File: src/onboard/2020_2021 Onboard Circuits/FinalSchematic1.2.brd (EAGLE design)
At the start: 137.6 x 80 mm, 82 parts, among them IC1 MIC2937A-5.0BT, IC3 A5975D

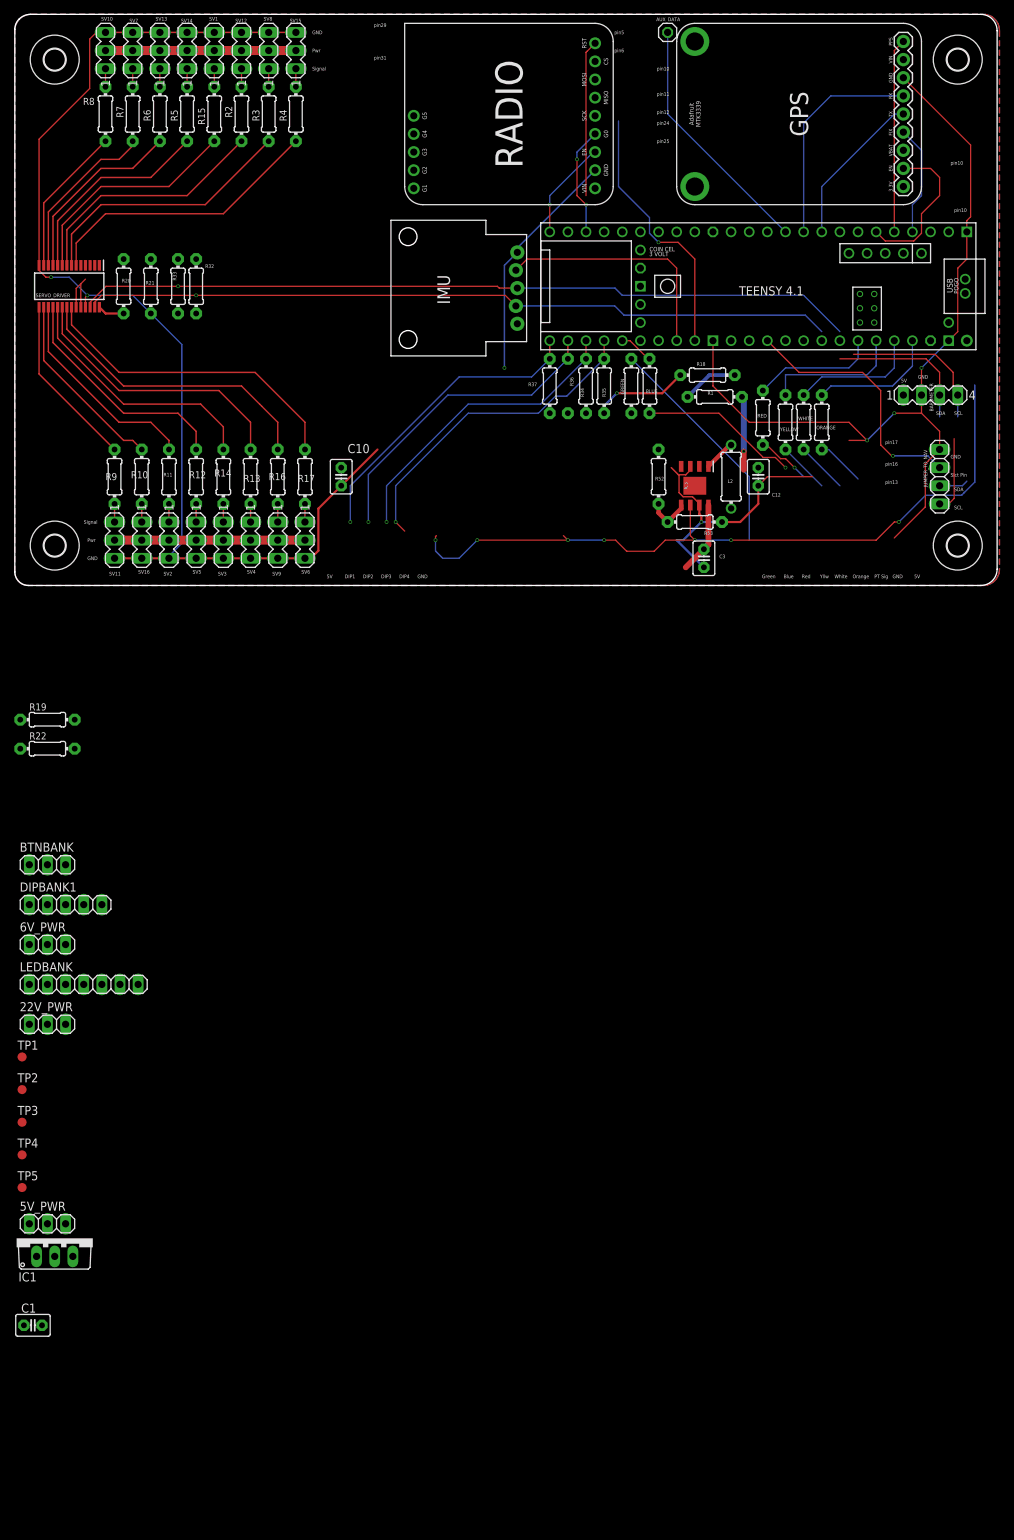
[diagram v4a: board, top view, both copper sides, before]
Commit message: Added pulldown on select pin and added wiring for aux pin
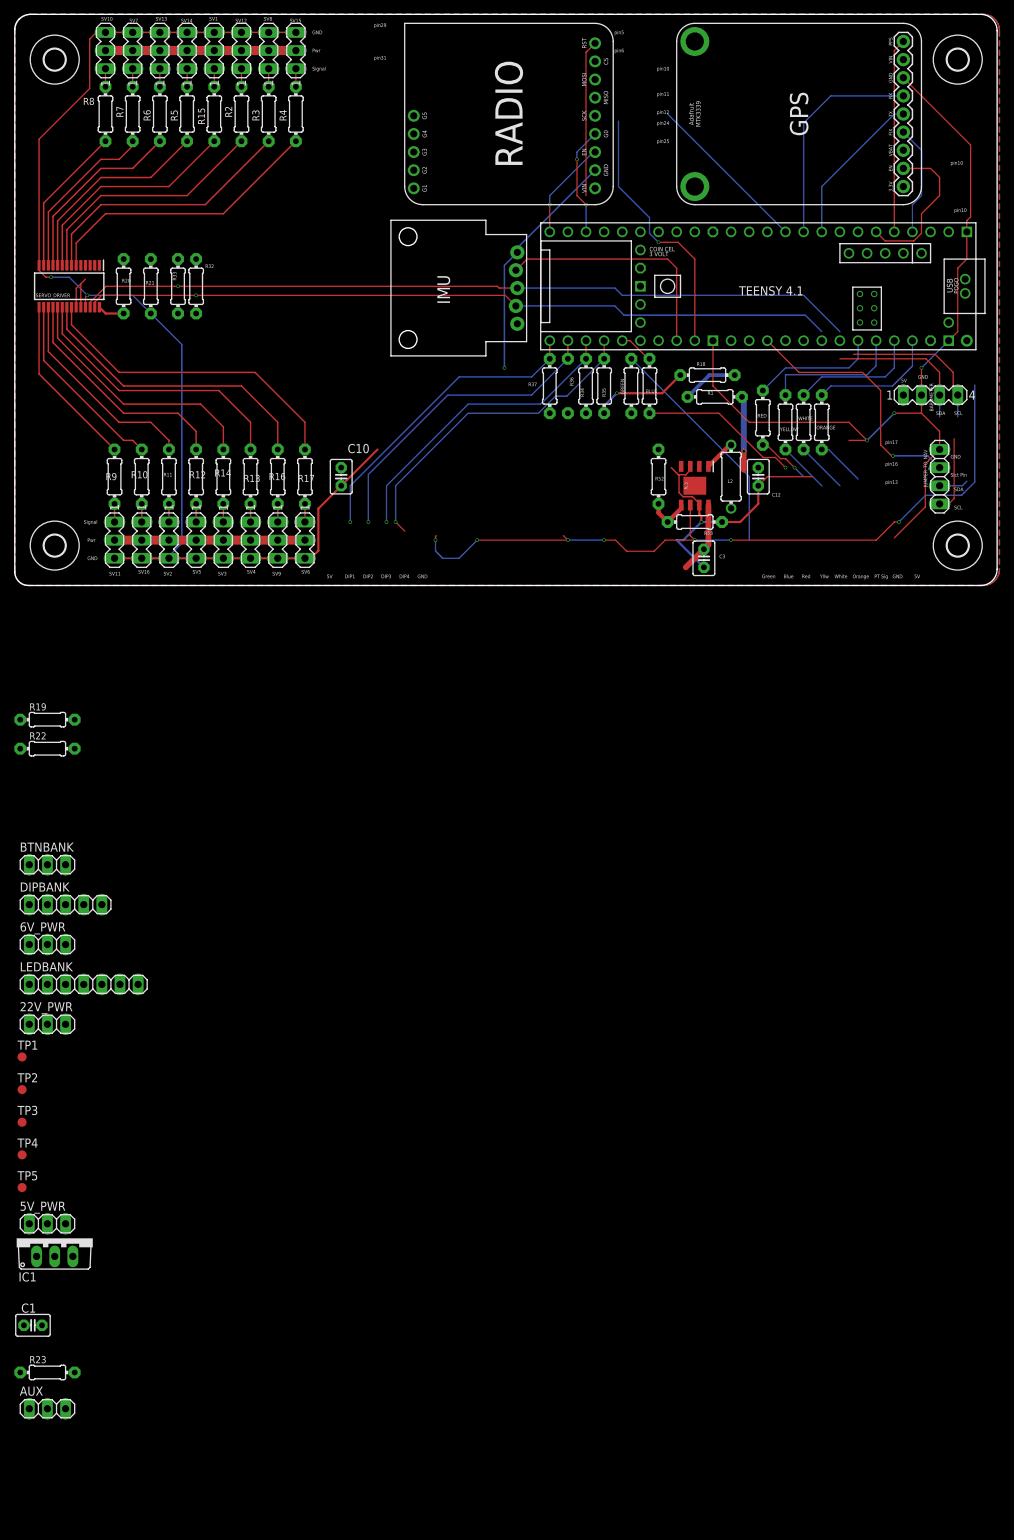
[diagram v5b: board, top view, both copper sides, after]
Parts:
- removed AUX_DATA: (no value), pinhead:1X01
- added AUX: (no value), pinhead:1X03
- added R23: 2.2k, adafruit:0204/7
- renumbered DIPBANK1 to DIPBANK
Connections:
- new net AUX: AUX.3, TEENSY4.1.27-A13/SCK1
- new net N$4: AUX.2
- net AUX_DATA: no longer AUX_DATA.1
- net GND: now also AUX.1, R23.1
- net SELECT_PIN: now also R23.2
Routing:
- net AUX_DATA: track 34.8 -> 23.3 mm
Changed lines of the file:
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@@
 <attribute name="VALUE" x="65.3596" y="13.4366" size="0.508" layer="27" ratio="10" rot="R180"/>
-</element>
-<element name="AUX_DATA" library="pinhead" library_urn="urn:adsk.eagle:library:325" package="1X01" package3d_urn="urn:adsk.eagle:package:22485/2" value="" x="55.88" y="77.47" smashed="yes" rot="R270">
-<attribute name="NAME" x="54.2798" y="79.0448" size="0.508" layer="25" ratio="10"/>
-<attribute name="POPULARITY" value="64" x="55.88" y="77.47" size="1.778" layer="27" rot="R270" display="off"/>
-<attribute name="VALUE" x="52.705" y="78.74" size="1.27" layer="27" rot="R270"/>
 </element>
 <element name="JUMPER_TO_NAV" library="pinhead" library_urn="urn:adsk.eagle:library:325" package="1X04" package3d_urn="urn:adsk.eagle:package:22407/2" value="" x="93.98" y="15.24" smashed="yes" rot="R270">
@@
 <attribute name="VALUE" x="-34.798" y="-42.291" size="1.27" layer="27"/>
 </element>
-<element name="DIPBANK1" library="pinhead" library_urn="urn:adsk.eagle:library:325" package="1X05" package3d_urn="urn:adsk.eagle:package:22469/2" value="" x="-28.448" y="-44.704" smashed="yes">
+<element name="DIPBANK" library="pinhead" library_urn="urn:adsk.eagle:library:325" package="1X05" package3d_urn="urn:adsk.eagle:package:22469/2" value="" x="-28.448" y="-44.704" smashed="yes">
 <attribute name="NAME" x="-34.8742" y="-42.8752" size="1.27" layer="25" ratio="10"/>
 <attribute name="POPULARITY" value="69" x="-28.448" y="-44.704" size="1.778" layer="27" display="off"/>
@@
 <attribute name="POPULARITY" value="38" x="-33.02" y="-103.632" size="1.778" layer="27" display="off"/>
 <attribute name="VALUE" x="-34.671" y="-106.68" size="1.27" layer="27" ratio="10"/>
+</element>
+<element name="R23" library="adafruit" library_urn="urn:adsk.eagle:library:420" package="0204/7" package3d_urn="urn:adsk.eagle:package:6240596/1" value="2.2k" x="-30.988" y="-110.236" smashed="yes">
+<attribute name="NAME" x="-33.528" y="-108.9406" size="0.9906" layer="25" ratio="12"/>
+<attribute name="VALUE" x="-32.6136" y="-110.7186" size="0.9906" layer="27" ratio="12"/>
+</element>
+<element name="AUX" library="pinhead" library_urn="urn:adsk.eagle:library:325" package="1X03" package3d_urn="urn:adsk.eagle:package:22458/2" value="" x="-30.988" y="-115.316" smashed="yes">
+<attribute name="NAME" x="-34.8742" y="-113.4872" size="1.27" layer="25" ratio="10"/>
+<attribute name="POPULARITY" value="92" x="-30.988" y="-115.316" size="1.778" layer="27" display="off"/>
+<attribute name="VALUE" x="-34.798" y="-118.491" size="1.27" layer="27"/>
 </element>
 </elements>
@@
 <contactref element="R33" pad="2"/>
 <contactref element="BTNBANK" pad="3"/>
-<contactref element="DIPBANK1" pad="5"/>
+<contactref element="DIPBANK" pad="5"/>
 <contactref element="SV9" pad="2"/>
 <contactref element="SV6" pad="2"/>
@@
 <wire x1="11.43" y1="13.97" x2="11.43" y2="8.89" width="0.1524" layer="16"/>
 <via x="11.43" y="8.89" extent="1-16" drill="0.35"/>
-<contactref element="DIPBANK1" pad="4"/>
+<contactref element="DIPBANK" pad="4"/>
 <wire x1="11.43" y1="8.89" x2="-25.908" y2="-44.704" width="0" layer="19" extent="1-1"/>
 </signal>
@@
 <via x="17.78" y="8.89" extent="1-16" drill="0.35"/>
 <wire x1="17.78" y1="8.89" x2="19.05" y2="7.62" width="0.1524" layer="1"/>
-<contactref element="DIPBANK1" pad="1"/>
+<contactref element="DIPBANK" pad="1"/>
 <wire x1="19.05" y1="7.62" x2="-33.528" y2="-44.704" width="0" layer="19" extent="1-1"/>
 </signal>
@@
 <wire x1="13.97" y1="15.55053125" x2="13.97" y2="8.89" width="0.1524" layer="16"/>
 <wire x1="36.83" y1="26.67" x2="25.08946875" y2="26.67" width="0.1524" layer="16"/>
-<contactref element="DIPBANK1" pad="3"/>
+<contactref element="DIPBANK" pad="3"/>
 <wire x1="13.97" y1="8.89" x2="-28.448" y2="-44.704" width="0" layer="19" extent="1-1"/>
 </signal>
@@
 <wire x1="16.51" y1="13.97" x2="16.51" y2="8.89" width="0.1524" layer="16"/>
 <via x="16.51" y="8.89" extent="1-16" drill="0.35"/>
-<contactref element="DIPBANK1" pad="2"/>
+<contactref element="DIPBANK" pad="2"/>
 <wire x1="16.51" y1="8.89" x2="-30.988" y2="-44.704" width="0" layer="19" extent="1-1"/>
 </signal>
@@
 <contactref element="5V_PWR" pad="3"/>
 <contactref element="IC1" pad="2"/>
+<contactref element="R23" pad="1"/>
+<contactref element="AUX" pad="1"/>
+<wire x1="-34.798" y1="-110.236" x2="-33.528" y2="-115.316" width="0" layer="19" extent="1-1"/>
+<wire x1="-29.972" y1="-93.98" x2="-34.798" y2="-110.236" width="0" layer="19" extent="1-1"/>
+<wire x1="-28.448" y1="-89.408" x2="-29.972" y2="-93.98" width="0" layer="19" extent="1-1"/>
+<wire x1="-28.448" y1="-61.468" x2="-28.448" y2="-89.408" width="0" layer="19" extent="1-1"/>
+<wire x1="-33.528" y1="-55.88" x2="-28.448" y2="-61.468" width="0" layer="19" extent="1-1"/>
+<wire x1="-28.448" y1="-50.292" x2="-33.528" y2="-55.88" width="0" layer="19" extent="1-1"/>
+<wire x1="-34.798" y1="-22.86" x2="-28.448" y2="-50.292" width="0" layer="19" extent="1-1"/>
+<wire x1="-34.798" y1="-18.796" x2="-34.798" y2="-22.86" width="0" layer="19" extent="1-1"/>
+<wire x1="-21.59" y1="3.81" x2="-34.798" y2="-18.796" width="0" layer="19" extent="1-1"/>
+<wire x1="33.02" y1="30.48" x2="15.24" y2="19.05" width="0" layer="19" extent="1-1"/>
+<wire x1="39.37" y1="24.13" x2="33.02" y2="30.48" width="0" layer="19" extent="1-1"/>
+<wire x1="41.91" y1="24.13" x2="39.37" y2="24.13" width="0" layer="19" extent="1-1"/>
+<wire x1="44.45" y1="24.13" x2="41.91" y2="24.13" width="0" layer="19" extent="1-1"/>
+<wire x1="46.99" y1="24.13" x2="44.45" y2="24.13" width="0" layer="19" extent="1-1"/>
+<wire x1="46.99" y1="25.146" x2="46.99" y2="24.13" width="0" layer="19" extent="16-16"/>
+<wire x1="62.23" y1="34.29" x2="57.658" y2="29.464" width="0" layer="19" extent="1-1"/>
+<wire x1="76.2" y1="15.24" x2="81.28" y2="20.32" width="0" layer="19" extent="1-1"/>
+<wire x1="52.07" y1="41.91" x2="62.23" y2="34.29" width="0" layer="19" extent="1-1"/>
+<wire x1="83.82" y1="46.53" x2="97.79" y2="49.53" width="0" layer="19" extent="1-1"/>
 <wire x1="81.28" y1="46.53" x2="83.82" y2="46.53" width="0" layer="19" extent="1-1"/>
-<wire x1="97.79" y1="49.53" x2="83.82" y2="46.53" width="0" layer="19" extent="1-1"/>
-<wire x1="57.658" y1="29.464" x2="62.23" y2="34.29" width="0" layer="19" extent="1-1"/>
-<wire x1="46.99" y1="24.13" x2="46.99" y2="25.146" width="0" layer="19" extent="16-16"/>
-<wire x1="44.45" y1="24.13" x2="46.99" y2="24.13" width="0" layer="19" extent="1-1"/>
-<wire x1="41.91" y1="24.13" x2="44.45" y2="24.13" width="0" layer="19" extent="1-1"/>
-<wire x1="39.37" y1="24.13" x2="41.91" y2="24.13" width="0" layer="19" extent="1-1"/>
-<wire x1="76.2" y1="15.24" x2="81.28" y2="20.32" width="0" layer="19" extent="1-1"/>
-<wire x1="33.02" y1="30.48" x2="39.37" y2="24.13" width="0" layer="19" extent="1-1"/>
-<wire x1="52.07" y1="41.91" x2="62.23" y2="34.29" width="0" layer="19" extent="1-1"/>
-<wire x1="15.24" y1="19.05" x2="33.02" y2="30.48" width="0" layer="19" extent="1-1"/>
-<wire x1="-34.798" y1="-18.796" x2="-21.59" y2="3.81" width="0" layer="19" extent="1-1"/>
-<wire x1="-34.798" y1="-22.86" x2="-34.798" y2="-18.796" width="0" layer="19" extent="1-1"/>
-<wire x1="-28.448" y1="-50.292" x2="-34.798" y2="-22.86" width="0" layer="19" extent="1-1"/>
-<wire x1="-33.528" y1="-55.88" x2="-28.448" y2="-50.292" width="0" layer="19" extent="1-1"/>
-<wire x1="-28.448" y1="-61.468" x2="-33.528" y2="-55.88" width="0" layer="19" extent="1-1"/>
-<wire x1="-28.448" y1="-89.408" x2="-28.448" y2="-61.468" width="0" layer="19" extent="1-1"/>
-<wire x1="-29.972" y1="-93.98" x2="-28.448" y2="-89.408" width="0" layer="19" extent="1-1"/>
 </signal>
 <signal name="GPS_EN">
@@
 </signal>
 <signal name="AUX_DATA">
-<contactref element="AUX_DATA" pad="1"/>
 <contactref element="TEENSY4.1" pad="9-OUT1C"/>
 <wire x1="72.39" y1="49.53" x2="55.88" y2="66.04" width="0.1524" layer="16"/>
-<wire x1="55.88" y1="66.04" x2="55.88" y2="77.47" width="0.1524" layer="16"/>
 </signal>
 <signal name="SELECT_PIN">
@@
 <wire x1="87.4381" y1="18.161" x2="92.329" y2="18.161" width="0.1524" layer="16"/>
 <wire x1="92.329" y1="18.161" x2="93.98" y2="16.51" width="0.1524" layer="16"/>
+<contactref element="R23" pad="2"/>
+<wire x1="87.4381" y1="18.161" x2="-27.178" y2="-110.236" width="0" layer="19" extent="1-1"/>
 </signal>
 <signal name="O_LED">
@@
 <wire x1="-30.988" y1="-50.292" x2="-33.528" y2="-50.292" width="0" layer="19" extent="1-1"/>
 </signal>
+<signal name="N$4">
+<contactref element="AUX" pad="2"/>
+</signal>
+<signal name="AUX">
+<contactref element="AUX" pad="3"/>
+<contactref element="TEENSY4.1" pad="27-A13/SCK1"/>
+<wire x1="52.07" y1="49.53" x2="-28.448" y2="-115.316" width="0" layer="19" extent="1-1"/>
+</signal>
 </signals>
